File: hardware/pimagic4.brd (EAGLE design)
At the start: 53.3 x 49.5 mm, 49 parts, among them IC1 ATMEGA328-P, Q1 2N7000, Q2 2N7000, U2 ARDUINO_SHIELDLONGPADS, Y1 16MHz

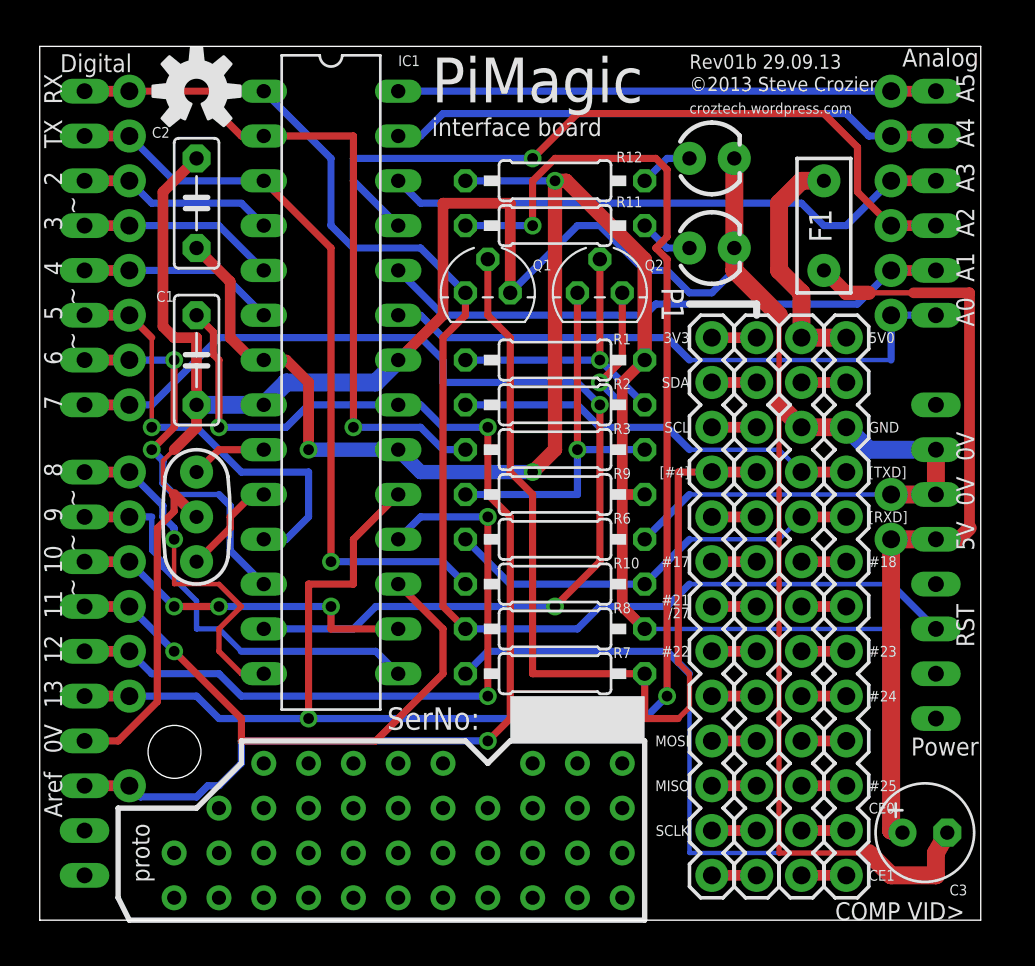
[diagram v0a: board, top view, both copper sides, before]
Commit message: Rev01c update
- Q1/Q2 silkscreen corrected
- some of the silkscreen logos are now corrected
- there’s a nice ground plan copper pour added on both sides
- files updated to Eagle 7.1.0 format
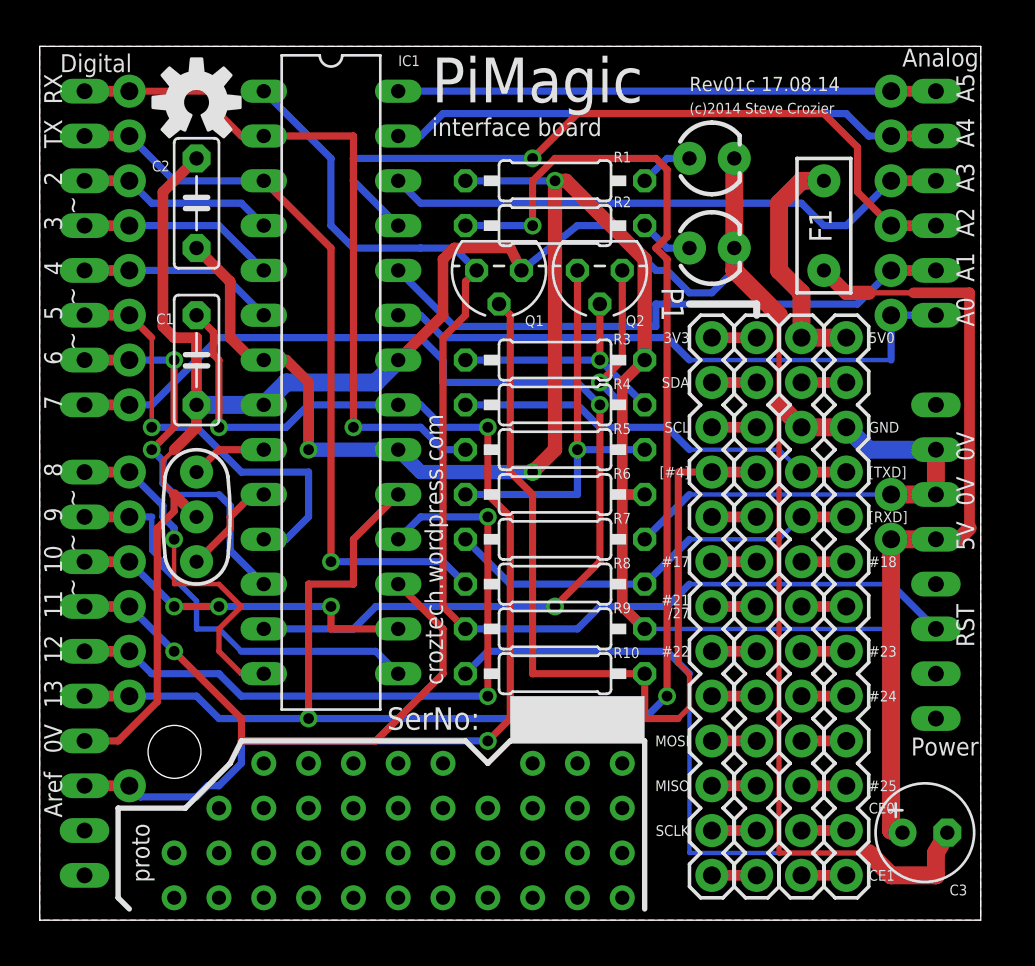
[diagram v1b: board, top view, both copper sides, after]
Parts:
- removed R11, R12: 220R, resistor:0207/10
- added R4, R5: 10K, resistor:0207/10
- IC1: value ATMEGA328-P -> ATMEGA328-PU
- LED1: value D13 -> PWR
- LED2: value PWR -> D13
- Q1, Q2: device transistor-fet:TO92 -> transistors:TO-92
- R1: value 4K7 -> 220R
- R10: value 12K -> 10K
- R2: value 10K -> 220R
- R3: value 10K -> 4K7
- R6: value 22K -> 1K
- R7: value 10K -> 22K
- R8: value 10K -> 12K
- R9: value 1K -> 10K
- moved R1 10.2 mm to (30.5, 71.1), turned to 180 degrees
- moved R9 10.2 mm to (30.5, 45.7)
- moved R2 10.2 mm to (30.5, 68.6), turned to 180 degrees
- moved R3 7.62 mm to (30.5, 61.0)
- moved R7 7.62 mm to (30.5, 50.8)
- moved R6 5.08 mm to (30.5, 55.9)
- moved LED1 5.08 mm to (39.4, 72.4)
- moved LED2 5.08 mm to (39.4, 67.3)
- moved R10 5.08 mm to (30.5, 43.2)
- moved R8 2.54 mm to (30.5, 48.3)
- moved Q1 1.42 mm to (27.3, 66.0), turned to 180 degrees
- moved Q2 1.27 mm to (33.0, 66.0), turned to 180 degrees
- moved U$1 0.64 mm to (10.2, 75.6)
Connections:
- net #4: now also R10.2; no longer R7.2
- net ARD_5V0: now also R5.2, R9.2; no longer R12.2, R8.2
- net ARD_RESET: now also R9.1; no longer R8.1
- net ARD_RXD: now also R6.1; no longer R9.1
- net ARD_TXD: now also R8.1; no longer R10.1
- net D13: now also R2.2; no longer R11.2
- net GND: now also R10.1, R7.2; no longer R6.2, R7.1
- net N$10: now also LED2.A, R2.1; no longer LED1.A, R11.1
- net N$12: now also LED1.A, R1.1; no longer LED2.A, R12.1
- net N$3: now also R3.1, R4.2; no longer R1.1, R2.2
- net N$7: now also R5.1, R6.2; no longer R3.1, R9.2
- net RXD: now also R7.1, R8.2; no longer R10.2, R6.1
- net TXD: now also R4.1; no longer R2.1
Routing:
- net GND: track 213.8 -> 206.0 mm
- net N$3: track 16.9 -> 14.4 mm
- net #4: track 54.3 -> 52.4 mm
- net ARD_RESET: track 67.3 -> 68.9 mm
- net N$7: track 21.6 -> 22.9 mm
- net TXD: track 31.8 -> 33.1 mm
- net A1: track 32.6 -> 33.9 mm
- added copper zone on layer 1, net GND
- added copper zone on layer 16, net GND
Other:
- board text added: "(c)2014 Steve Crozier"
- board text added: "Rev01c 17.08.14"
- board text removed: "COMP VID>"
- board text removed: "Rev01b 29.09.13"
- board text removed: "©2013 Steve Crozier"
